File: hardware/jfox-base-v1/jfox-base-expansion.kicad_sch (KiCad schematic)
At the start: 3 parts, among them J100 EXP A, J101 EXP B, J102 EXP C

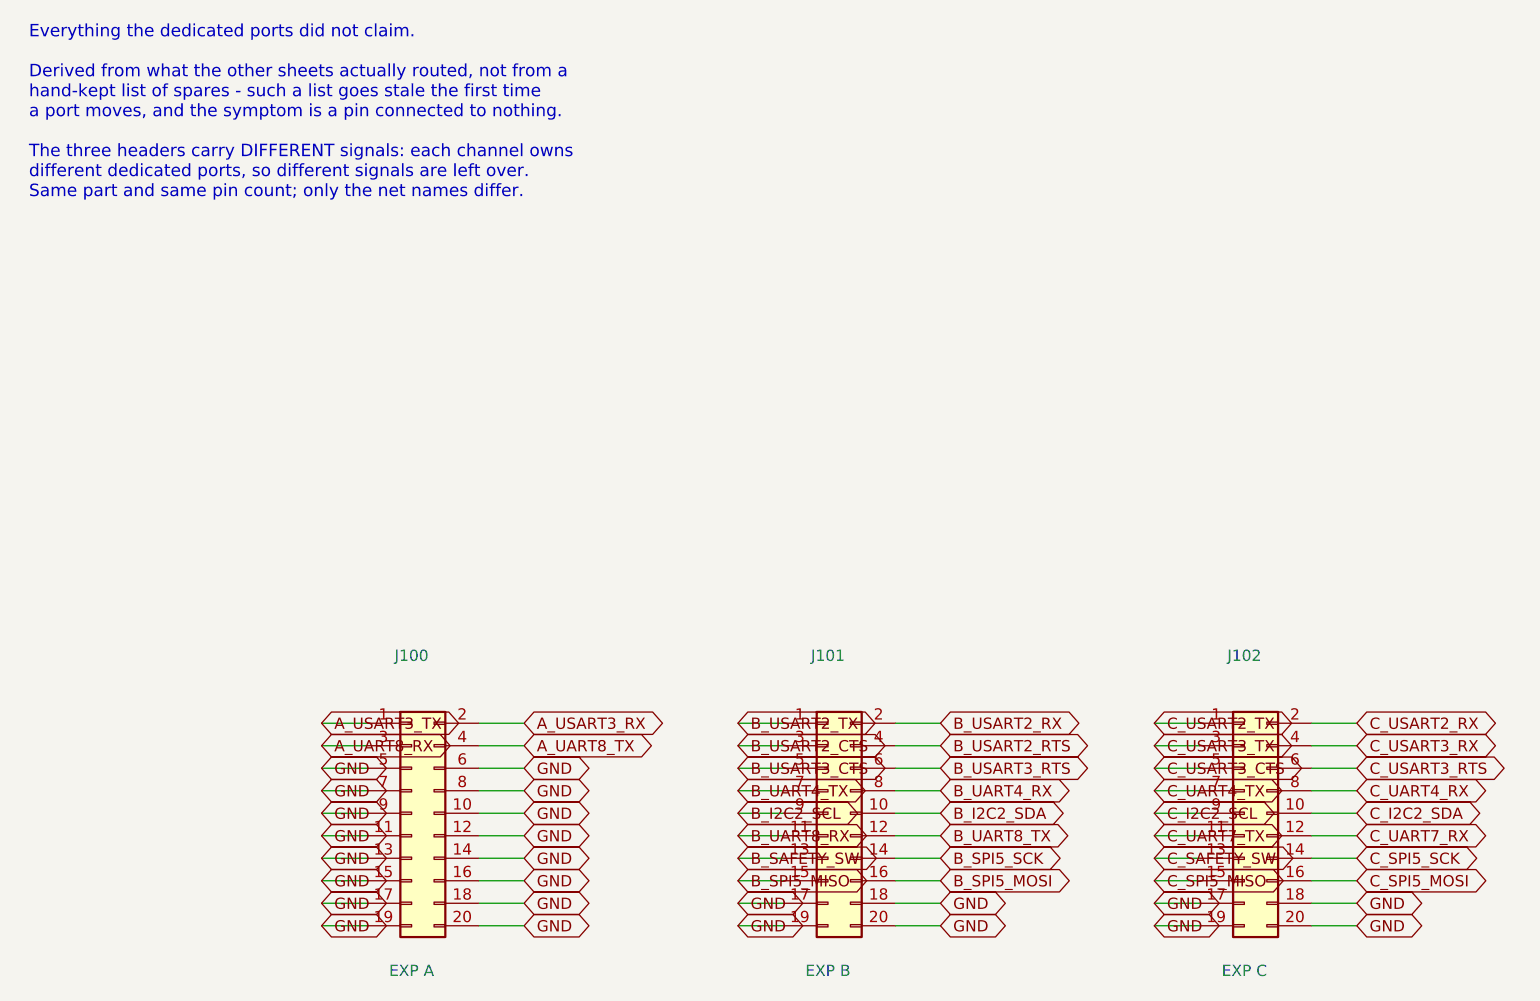
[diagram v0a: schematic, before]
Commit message: LTC4417 lands on the backplane, replacing the diode OR
It left the FCU when the power tree moved and never arrived here - the
backplane has been ORing its two airframe feeds with a pair of Schottkys,
which works and throws away the two things the part was chosen for:

  * Priority. A diode OR takes whichever feed is momentarily higher, so two
    supplies sitting 100 mV apart make the board chatter between them. The
    LTC4417 holds its selection until that source leaves its window.
  * A window. Under- and over-voltage per input, so a feed that has drifted
    out of spec is rejected rather than used because it is the higher of two
    bad ones.

It also drops ~0.4 V across a 5 V rail that the PMOS pass devices do not.

Two inputs, not three. V3 is tied to ground and its pass FET omitted, which
is how the datasheet says to leave an input out; inventing a third feed to
fill it would be worse. D50/D51 stay as reverse-polarity protection.

Three faults surfaced while wiring it, none of them the ORing:

  * The actuator headers still asked each channel for VDD_SERVO. That rail
    left the card's pinout when the power tree moved - servo power now runs
    from the backplane straight to the actuators and never passes through a
    card, which is the right way round. Three nets had nothing driving them.
  * EN was tied to +3V3, a rail the backplane does not have. It regulates
    nothing; the cards do. Now tied to the primary feed, so the part is
    enabled whenever there is power at all.
  * The expansion header overflowed. Its guard reported "25 spare signals
    will not fit a 20-pin header - widen it rather than dropping the
    overflow silently", which is exactly what it was written to catch. 2x15.

The far-face hole check earned itself again: a threshold divider placed on
the back landed under a card socket's through-holes. Bands on the back face
have to thread between sockets at y 20..27, 46..53 and 72..79.

  FCU        DRC 0 blocking, 105 parts, all checks pa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
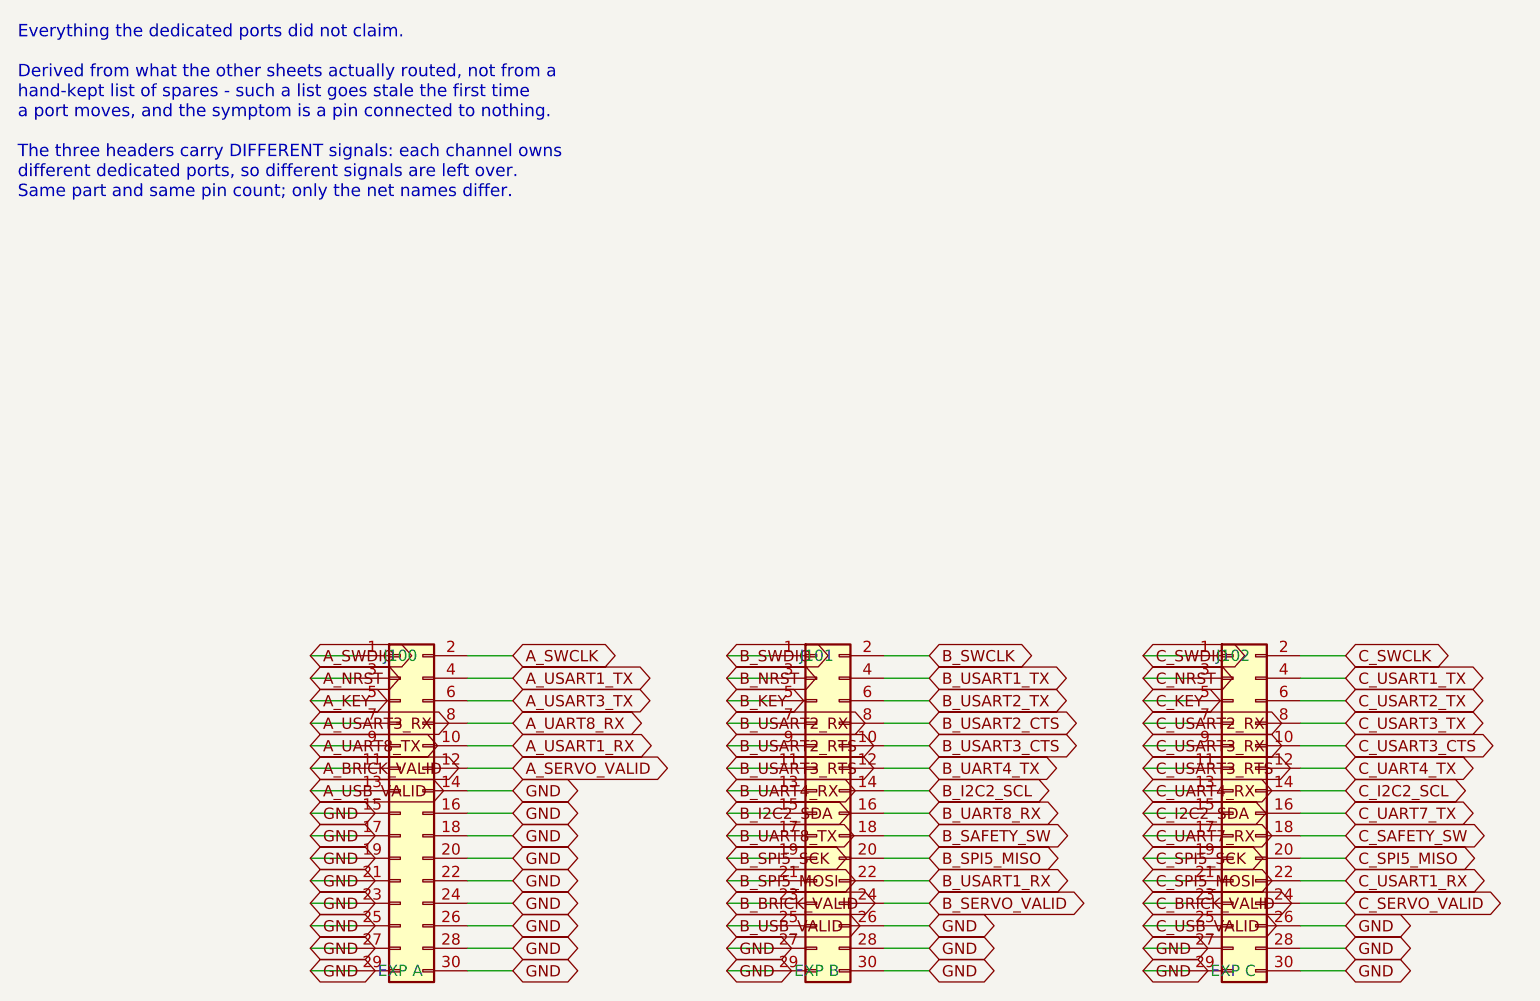
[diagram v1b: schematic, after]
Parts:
- removed J100: EXP A, Connector_PinHeader_1.27mm:PinHeader_2x10_P1.27mm_Vertical_SMD, symbol Connector_Generic:Conn_02x10_Odd_Even
- removed J101: EXP B, Connector_PinHeader_1.27mm:PinHeader_2x10_P1.27mm_Vertical_SMD, symbol Connector_Generic:Conn_02x10_Odd_Even
- removed J102: EXP C, Connector_PinHeader_1.27mm:PinHeader_2x10_P1.27mm_Vertical_SMD, symbol Connector_Generic:Conn_02x10_Odd_Even
- added J100: EXP A, Connector_PinHeader_1.27mm:PinHeader_2x10_P1.27mm_Vertical_SMD, symbol Connector_Generic:Conn_02x15_Odd_Even
- added J101: EXP B, Connector_PinHeader_1.27mm:PinHeader_2x10_P1.27mm_Vertical_SMD, symbol Connector_Generic:Conn_02x15_Odd_Even
- added J102: EXP C, Connector_PinHeader_1.27mm:PinHeader_2x10_P1.27mm_Vertical_SMD, symbol Connector_Generic:Conn_02x15_Odd_Even
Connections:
- net A_UART8_RX: now also J100.8 (Pin_8)
- net A_UART8_TX: now also J100.9 (Pin_9)
- net A_USART3_RX: now also J100.7 (Pin_7)
- net A_USART3_TX: now also J100.6 (Pin_6)
- net B_I2C2_SCL: now also J101.14 (Pin_14)
- net B_I2C2_SDA: now also J101.15 (Pin_15)
- net B_SAFETY_SW: now also J101.18 (Pin_18)
- net B_SPI5_MISO: now also J101.20 (Pin_20)
- net B_SPI5_MOSI: now also J101.21 (Pin_21)
- net B_SPI5_SCK: now also J101.19 (Pin_19)
- net B_UART4_RX: now also J101.13 (Pin_13)
- net B_UART4_TX: now also J101.12 (Pin_12)
- net B_UART8_RX: now also J101.16 (Pin_16)
- net B_UART8_TX: now also J101.17 (Pin_17)
- net B_USART2_CTS: now also J101.8 (Pin_8)
- net B_USART2_RTS: now also J101.9 (Pin_9)
- net B_USART2_RX: now also J101.7 (Pin_7)
- net B_USART2_TX: now also J101.6 (Pin_6)
- net B_USART3_CTS: now also J101.10 (Pin_10)
- net B_USART3_RTS: now also J101.11 (Pin_11)
- net C_I2C2_SCL: now also J102.14 (Pin_14)
- net C_I2C2_SDA: now also J102.15 (Pin_15)
- net C_SAFETY_SW: now also J102.18 (Pin_18)
- net C_SPI5_MISO: now also J102.20 (Pin_20)
- net C_SPI5_MOSI: now also J102.21 (Pin_21)
- net C_SPI5_SCK: now also J102.19 (Pin_19)
- net C_UART4_RX: now also J102.13 (Pin_13)
- net C_UART4_TX: now also J102.12 (Pin_12)
- net C_UART7_RX: now also J102.17 (Pin_17)
- net C_UART7_TX: now also J102.16 (Pin_16)
- net C_USART2_RX: now also J102.7 (Pin_7)
- net C_USART2_TX: now also J102.6 (Pin_6)
- net C_USART3_CTS: now also J102.10 (Pin_10)
- net C_USART3_RTS: now also J102.11 (Pin_11)
- net C_USART3_RX: now also J102.9 (Pin_9)
- net C_USART3_TX: now also J102.8 (Pin_8)
- net GND: now also J100.14 (Pin_14), J100.15 (Pin_15), J100.16 (Pin_16), J100.17 (Pin_17), J100.18 (Pin_18), J100.19 (Pin_19), J100.20 (Pin_20), J100.21 (Pin_21), J100.22 (Pin_22), J100.23 (Pin_23), J100.24 (Pin_24), J100.25 (Pin_25), J100.26 (Pin_26), J100.27 (Pin_27), J100.28 (Pin_28), J100.29 (Pin_29), J100.30 (Pin_30), J101.26 (Pin_26), J101.27 (Pin_27), J101.28 (Pin_28), J101.29 (Pin_29), J101.30 (Pin_30), J102.26 (Pin_26), J102.27 (Pin_27), J102.28 (Pin_28), J102.29 (Pin_29), J102.30 (Pin_30)
- new net A_BRICK_VALID: J100.11 (Pin_11)
- new net A_KEY: J100.5 (Pin_5)
- new net A_NRST: J100.3 (Pin_3)
- new net A_SERVO_VALID: J100.12 (Pin_12)
- new net A_SWCLK: J100.2 (Pin_2)
- new net A_SWDIO: J100.1 (Pin_1)
- new net A_USART1_RX: J100.10 (Pin_10)
- new net A_USART1_TX: J100.4 (Pin_4)
- new net A_USB_VALID: J100.13 (Pin_13)
- new net B_BRICK_VALID: J101.23 (Pin_23)
- new net B_KEY: J101.5 (Pin_5)
- new net B_NRST: J101.3 (Pin_3)
- new net B_SERVO_VALID: J101.24 (Pin_24)
- new net B_SWCLK: J101.2 (Pin_2)
- new net B_SWDIO: J101.1 (Pin_1)
- new net B_USART1_RX: J101.22 (Pin_22)
- new net B_USART1_TX: J101.4 (Pin_4)
- new net B_USB_VALID: J101.25 (Pin_25)
- new net C_BRICK_VALID: J102.23 (Pin_23)
- new net C_KEY: J102.5 (Pin_5)
- new net C_NRST: J102.3 (Pin_3)
- new net C_SERVO_VALID: J102.24 (Pin_24)
- new net C_SWCLK: J102.2 (Pin_2)
- new net C_SWDIO: J102.1 (Pin_1)
- new net C_USART1_RX: J102.22 (Pin_22)
- new net C_USART1_TX: J102.4 (Pin_4)
- new net C_USB_VALID: J102.25 (Pin_25)

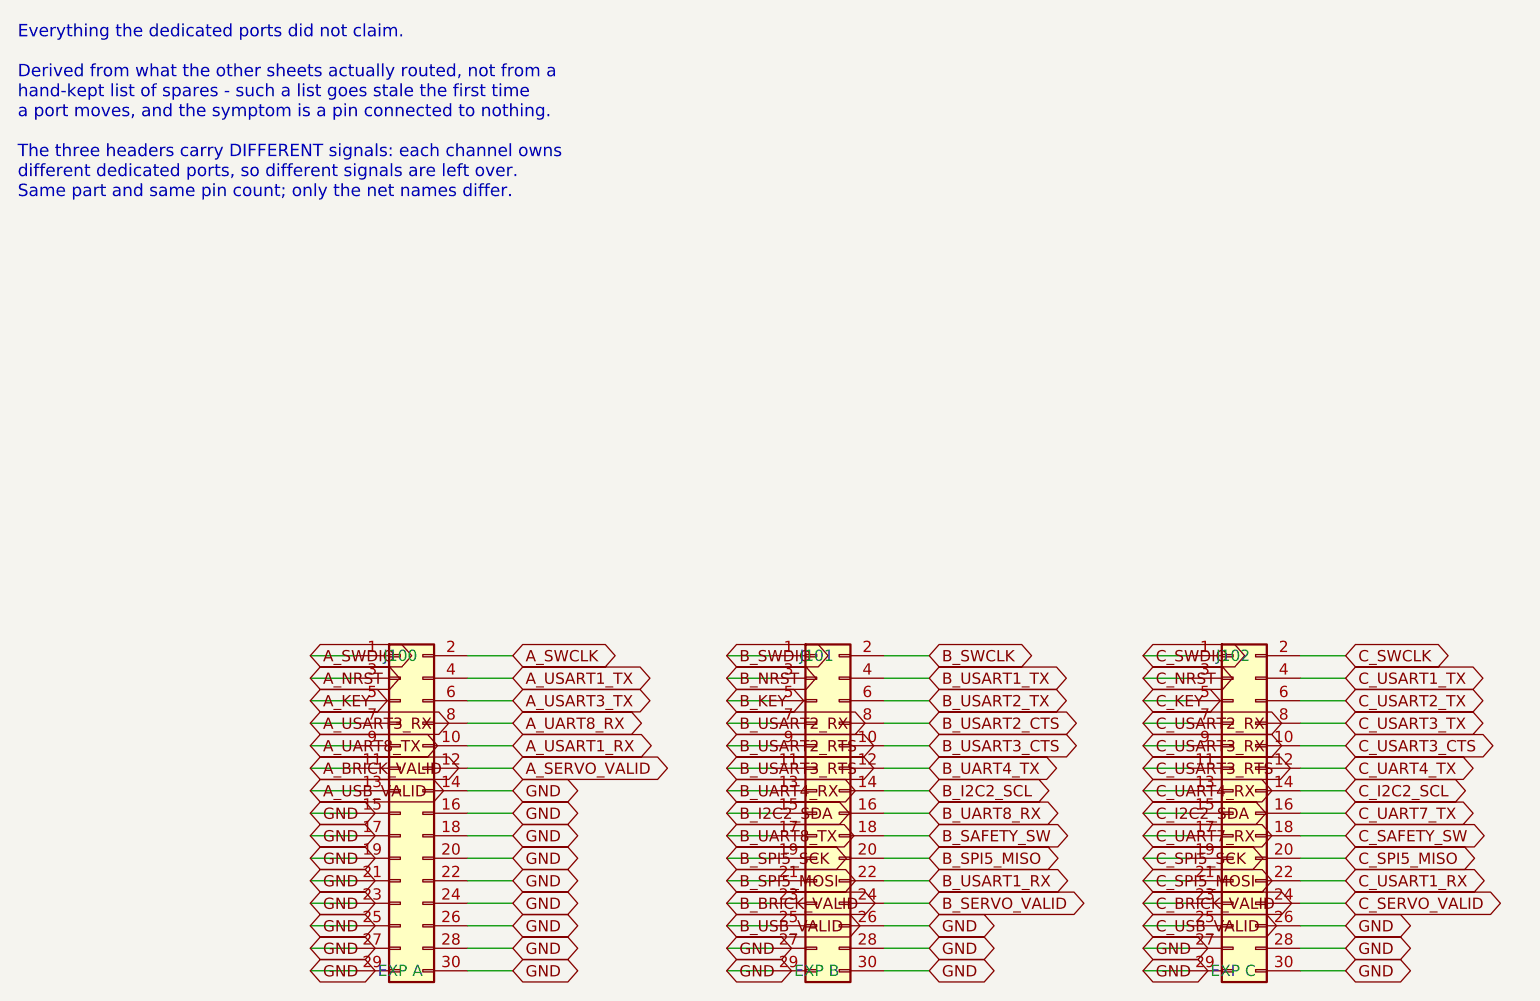
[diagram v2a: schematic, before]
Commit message: Provability: check the backplane, and fix the four defects that found
Nothing read JFOX-BASE-v1. Every checker in hardware/tools/ opened
jfox-fmu-v1/jfox-fmu.kicad_sch and only that, so no claim about the
backplane was provable - including the ones the requirements table recorded
as verified.

check_base_schematic.py now reads it: fused rails must reach a card socket,
the LTC4417 divider must produce the window it claims, that window must fit
every part downstream, and the feed-health outputs must reach a card AND be
driven. It failed on first run, which is the only reason to trust it.

What it found, in the order it found them:

  1. THE CARDS HAD NO POWER. The fuses put out A/B/C_FUSED and the card edge
     reads +5V_CARRIER. Both boards generated cleanly, both passed DRC, and
     the two halves were never connected to each other. The chain now
     terminates on the card rail past the shunt, not before it.

  2. THE FEEDS ARE NOT BATTERIES. VBAT_RH/VBAT_LH carry 5 V - the thresholds
     said so and the connectors are labelled PWR. Renamed PWR1_IN/PWR2_IN,
     output PWR_ORED. The name was the thing that was wrong.

  3. THE WINDOW PASSED MORE THAN A PART SURVIVES, and the binding part was
     not the one found by hand. The analysis flagged the AP2112K at 6.0 V
     against a 5.81 V threshold - 190 mV. The checker compared against every
     downstream part and found the ISOW1044 at 5.5 V: NEGATIVE 310 mV. A
     feed the controller reported as good would have destroyed the isolator.

     787k / 28k7 / 196k -> UV 4.50 V, OV 5.16 V
       ISOW1044  +338 mV      AP2112K  +838 mV

  4. THE ORING CONTROLLER'S OUTPUT WAS NEVER CONNECTED. Its pin map was
     written from the datasheet's block diagram, not the symbol: the pins
     are ~{VALID1..3} with overbars, VOUT not OUT, HYS not HYST, and there
     is no STAT pin at all. nets.get() returns None for an unknown key, so
     six pins were silently left unwired - VOUT among them. PWR_ORED was fed
     only by D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
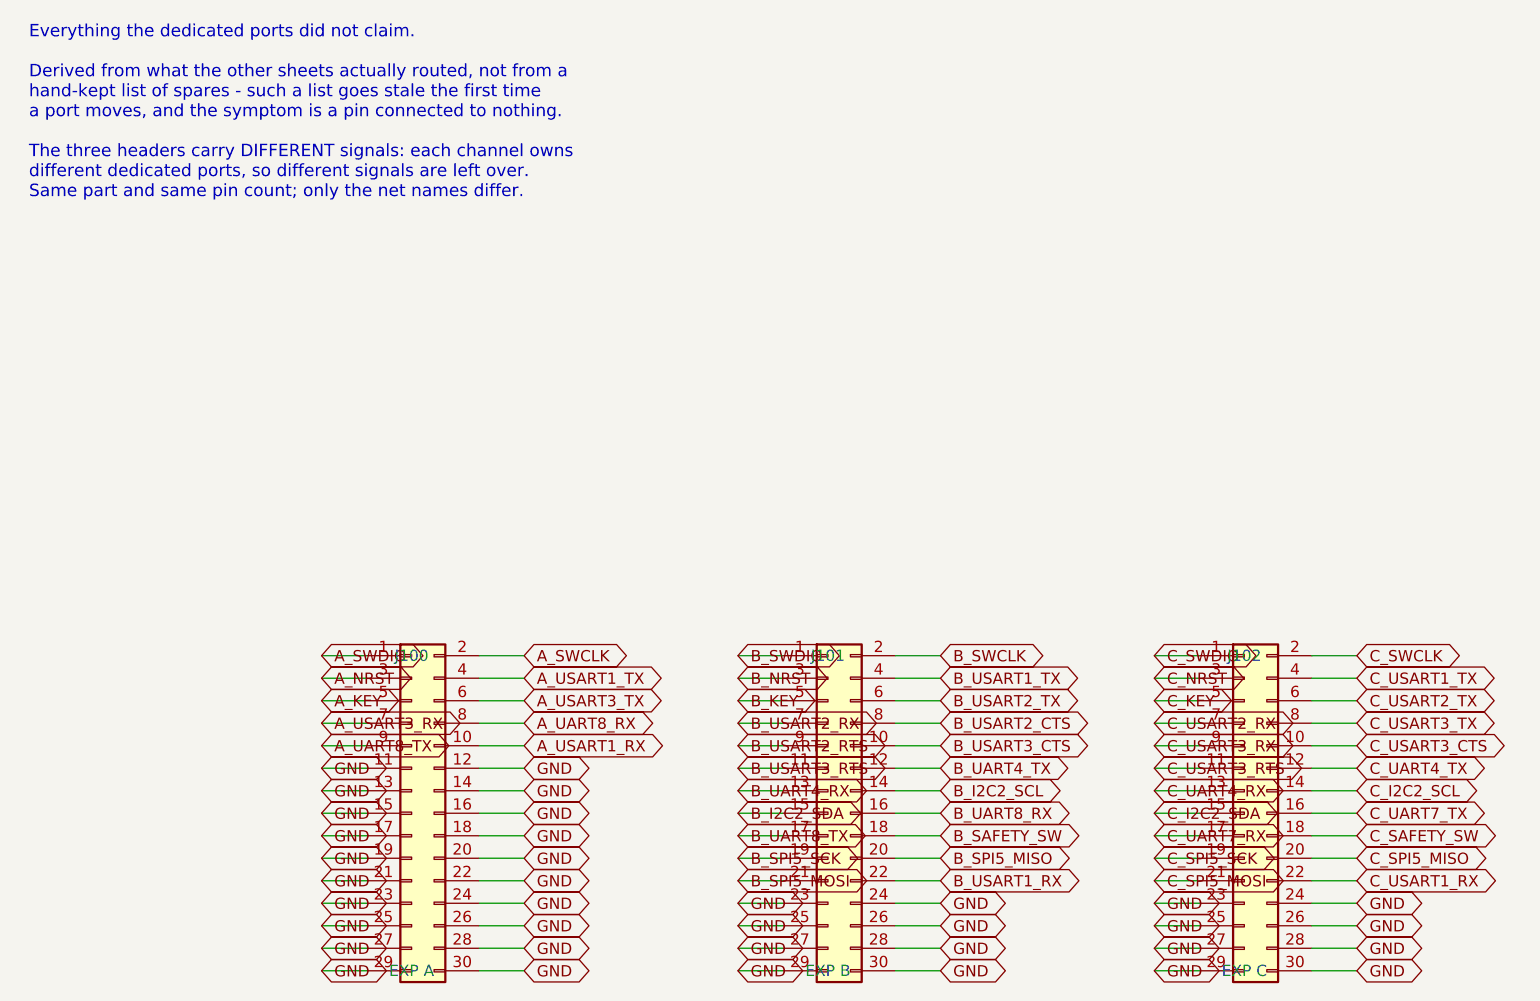
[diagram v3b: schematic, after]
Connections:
- net A_BRICK_VALID is gone; now on net GND: J100.11 (Pin_11)
- net A_SERVO_VALID is gone; now on net GND: J100.12 (Pin_12)
- net A_USB_VALID is gone; now on net GND: J100.13 (Pin_13)
- net B_BRICK_VALID is gone; now on net GND: J101.23 (Pin_23)
- net B_SERVO_VALID is gone; now on net GND: J101.24 (Pin_24)
- net B_USB_VALID is gone; now on net GND: J101.25 (Pin_25)
- net C_BRICK_VALID is gone; now on net GND: J102.23 (Pin_23)
- net C_SERVO_VALID is gone; now on net GND: J102.24 (Pin_24)
- net C_USB_VALID is gone; now on net GND: J102.25 (Pin_25)
